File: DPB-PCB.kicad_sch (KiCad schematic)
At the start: 2 parts, among them J1 USB-C, U1 ESP32-S3-WROOM-1-N4R2

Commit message: up
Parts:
- removed J1: USB-C, Library:MOLEX_USB_TYPE_C, symbol MOLEX_USB_TYPE_C:105450-0101
- added Q1: MMBT5551L, Package_TO_SOT_SMD:SOT-23, symbol Transistor_BJT:MMBT5551L
- U1: LCSC (none) -> C2913204; MANUFACTURER Espressif -> (none); MAXIMUM_PACKAGE_HEIGHT 3.25mm -> (none); PARTREV v1.0 -> (none); STANDARD Manufacturer Recommendations -> (none)
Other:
- added sheet Connections (Connections.kicad_sch)
- added sheet Power Supply (PowerSupply.kicad_sch)
- company: (none) -> V2
- title: (none) -> Dynamic propeller balancer
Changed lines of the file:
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@@
 (kicad_sch (version 20230121) (generator eeschema)
   (paper "A4")
-  (symbol (lib_id "MOLEX_USB_TYPE_C:105450-0101") (at 74.93 82.55 0) (unit 1)
-    (in_bom yes) (on_board yes) (dnp no) (fields_autoplaced)
-    (property "Reference" "J1" (at 74.93 63.5 0)
-      (effects (font (size 1.27 1.27)))
-    )
-    (property "Value" "USB-C" (at 74.93 66.04 0)
-      (effects (font (size 1.27 1.27)))
-    )
-    (property "Footprint" "Library:MOLEX_USB_TYPE_C" (at 74.93 82.55 0)
-      (effects (font (size 1.27 1.27)) (justify bottom) hide)
-    )
-    (property "Datasheet" "" (at 74.93 82.55 0)
-      (effects (font (size 1.27 1.27)) hide)
-    )
-    (property "STANDARD" "Manufacturer Recommendations" (at 74.93 82.55 0)
-      (effects (font (size 1.27 1.27)) (justify bottom) hide)
-    )
-    (property "PARTREV" "A7" (at 74.93 82.55 0)
-      (effects (font (size 1.27 1.27)) (justify bottom) hide)
-    )
-    (property "MANUFACTURER" "Molex" (at 74.93 82.55 0)
-      (effects (font (size 1.27 1.27)) (justify bottom) hide)
-    )
-    (property "MAXIMUM_PACKAGE_HEIGHT" "3.24mm" (at 74.93 82.55 0)
-      (effects (font (size 1.27 1.27)) (justify bottom) hide)
-    )
-    (pin "A1")
-    (pin "A10")
-    (pin "A11")
-    (pin "A12")
-    (pin "A2")
-    (pin "A3")
-    (pin "A4")
-    (pin "A5")
-    (pin "A6")
-    (pin "A7")
-    (pin "A8")
-    (pin "A9")
-    (pin "B1")
-    (pin "B10")
-    (pin "B11")
-    (pin "B12")
-    (pin "B2")
-    (pin "B3")
-    (pin "B4")
-    (pin "B5")
-    (pin "B6")
-    (pin "B7")
-    (pin "B8")
-    (pin "B9")
-    (pin "S1")
-    (pin "S2")
-    (pin "S3")
-    (pin "S4")
-    (instances
-      (project "DPB-PCB"
-        (path "/0a09ce58-c923-4e96-b56b-0b86aca559ed"
-          (reference "J1") (unit 1)
-        )
-      )
-    )
+  (title_block
+    (title "Dynamic propeller balancer")
+    (date "2023-02-27")
+    (rev "1")
+    (company "V2")
   )
   (symbol (lib_id "ESP32-S3-WROOM-1-N4R2:ESP32-S3-WROOM-1-N4R2") (at 138.43 101.6 0) (unit 1)
@@
       (effects (font (size 1.27 1.27)) hide)
     )
-    (property "PARTREV" "v1.0" (at 138.43 101.6 0)
-      (effects (font (size 1.27 1.27)) (justify bottom) hide)
-    )
-    (property "MANUFACTURER" "Espressif" (at 138.43 101.6 0)
-      (effects (font (size 1.27 1.27)) (justify bottom) hide)
-    )
-    (property "MAXIMUM_PACKAGE_HEIGHT" "3.25mm" (at 138.43 101.6 0)
-      (effects (font (size 1.27 1.27)) (justify bottom) hide)
-    )
-    (property "STANDARD" "Manufacturer Recommendations" (at 138.43 101.6 0)
-      (effects (font (size 1.27 1.27)) (justify bottom) hide)
+    (property "LCSC" "C2913204" (at 138.43 101.6 0)
+      (effects (font (size 1.27 1.27)) hide)
     )
     (pin "1")
@@
       )
     )
+  )
+  (symbol (lib_id "Transistor_BJT:MMBT5551L") (at 189.23 81.28 0) (unit 1)
+    (in_bom yes) (on_board yes) (dnp no) (fields_autoplaced)
+    (property "Reference" "Q1" (at 194.31 80.645 0)
+      (effects (font (size 1.27 1.27)) (justify left))
+    )
+    (property "Value" "MMBT5551L" (at 194.31 83.185 0)
+      (effects (font (size 1.27 1.27)) (justify left))
+    )
+    (property "Footprint" "Package_TO_SOT_SMD:SOT-23" (at 194.31 83.185 0)
+      (effects (font (size 1.27 1.27) italic) (justify left) hide)
+    )
+    (property "Datasheet" "www.onsemi.com/pub/Collateral/MMBT5550LT1-D.PDF" (at 189.23 81.28 0)
+      (effects (font (size 1.27 1.27)) (justify left) hide)
+    )
+    (property "LCSC" "" (at 189.23 81.28 0)
+      (effects (font (size 1.27 1.27)) hide)
+    )
+    (pin "1")
+    (pin "2")
+    (pin "3")
+    (instances
+      (project "DPB-PCB"
+        (path "/0a09ce58-c923-4e96-b56b-0b86aca559ed"
+          (reference "Q1") (unit 1)
+        )
+      )
+    )
+  )
+  (sheet (at 17.78 17.78) (size 19.05 11.43) (fields_autoplaced)
+    (stroke (width 0.1524) (type solid))
+    (fill (color 0 0 0 0.0000))
+    (property "Sheetname" "Power Supply" (at 17.78 17.0684 0)
+      (effects (font (size 1.27 1.27)) (justify left bottom))
+    )
+    (property "Sheetfile" "PowerSupply.kicad_sch" (at 17.78 29.7946 0)
+      (effects (font (size 1.27 1.27)) (justify left top))
+    )
+    (instances
+      (project "DPB-PCB"
+        (path "/0a09ce58-c923-4e96-b56b-0b86aca559ed" (page "2"))
+      )
+    )
+  )
+  (sheet (at 53.34 17.78) (size 22.86 11.43) (fields_autoplaced)
+    (stroke (width 0.1524) (type solid))
+    (fill (color 0 0 0 0.0000))
+    (property "Sheetname" "Connections" (at 53.34 17.0684 0)
+      (effects (font (size 1.27 1.27)) (justify left bottom))
+    )
+    (property "Sheetfile" "Connections.kicad_sch" (at 53.34 29.7946 0)
+      (effects (font (size 1.27 1.27)) (justify left top))
+    )
+    (instances
+      (project "DPB-PCB"
+        (path "/0a09ce58-c923-4e96-b56b-0b86aca559ed" (page "3"))
+      )
+    )

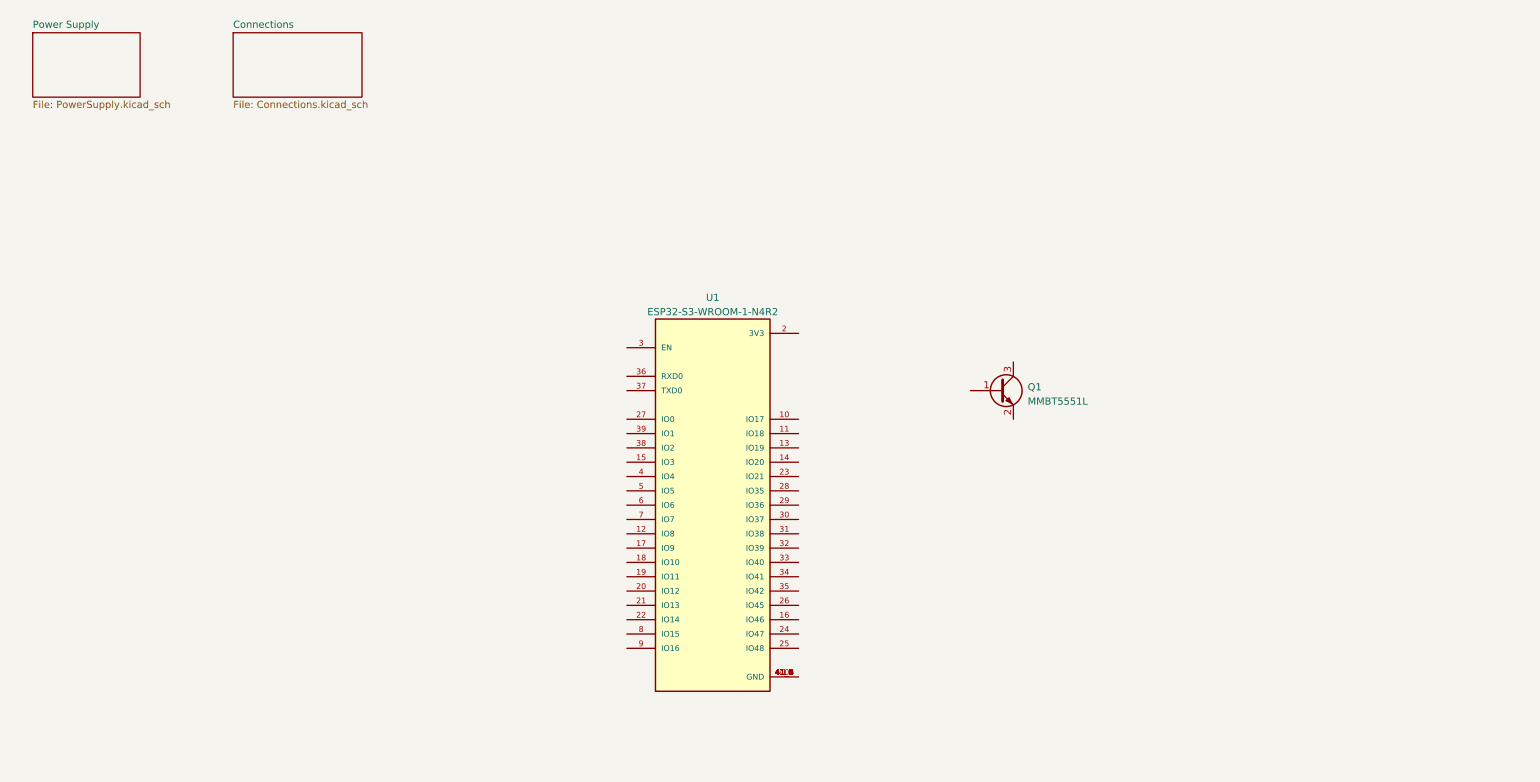
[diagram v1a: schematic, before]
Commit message: All components have been added
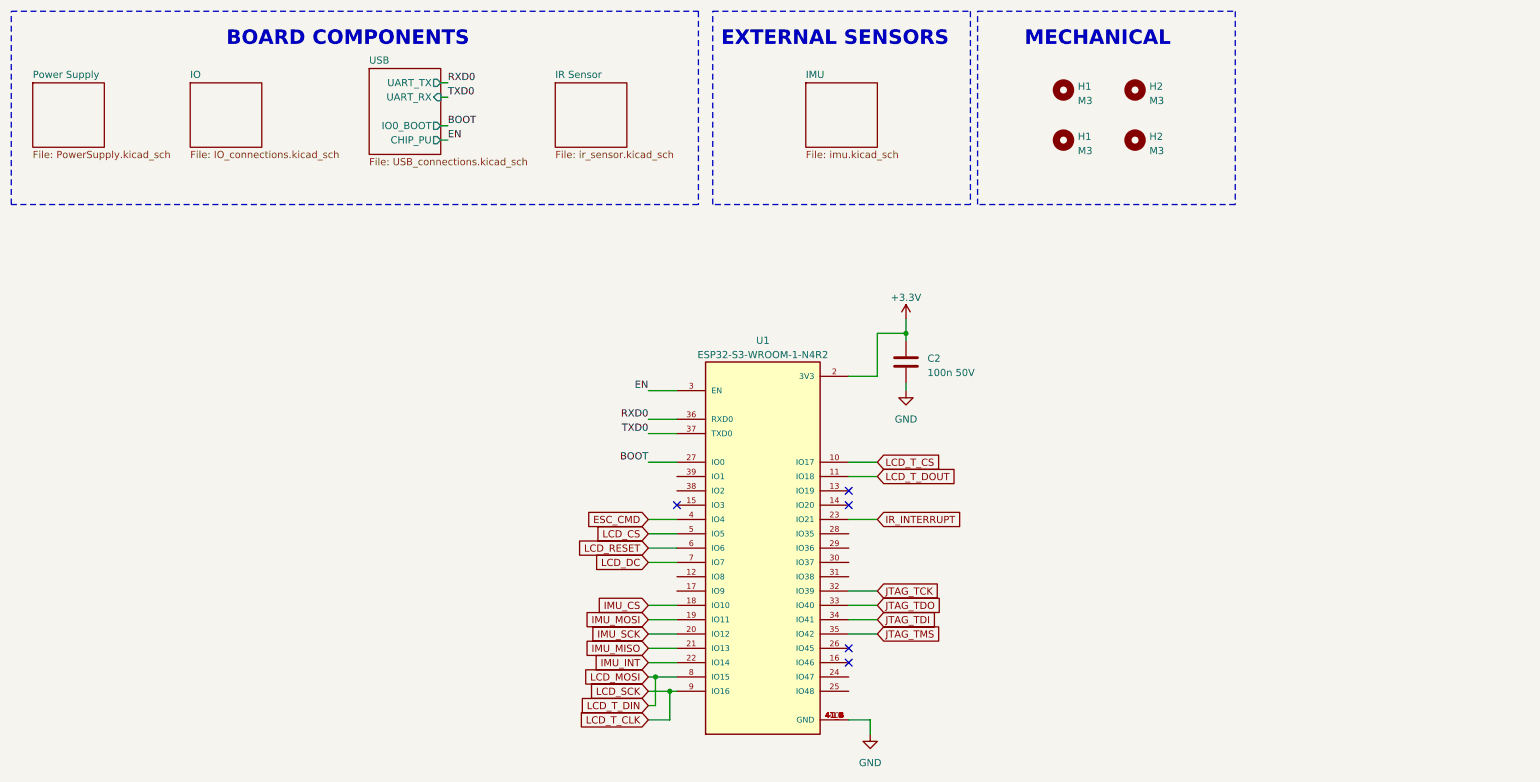
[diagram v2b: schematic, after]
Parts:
- removed Q1: MMBT5551L, Package_TO_SOT_SMD:SOT-23, symbol Transistor_BJT:MMBT5551L
- added C2: 100n 50V, Capacitor_SMD:C_01005_0402Metric, symbol Device:C
- added H1 (x2), H2 (x2): M3, MountingHole:MountingHole_3.2mm_M3_Pad_TopBottom, symbol Mechanical:MountingHole
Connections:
- net GND: now reaches U1.1 (GND), U1.40 (GND), U1.41_1 (GND), U1.41_2 (GND), U1.41_3 (GND), U1.41_4 (GND), U1.41_5 (GND), U1.41_6 (GND), U1.41_7 (GND), U1.41_8 (GND), U1.41_9 (GND)
- net GND: now also C2.2
- net LCD_T_CS: now reaches U1.10 (IO17)
- net LCD_T_DOUT: now reaches U1.11 (IO18)
- net IMU_CS: now reaches U1.18 (IO10)
- net IMU_MOSI: now reaches U1.19 (IO11)
- net +3.3V: now reaches U1.2 (3V3)
- net +3.3V: now also C2.1
- net IMU_SCK: now reaches U1.20 (IO12)
- net IMU_MISO: now reaches U1.21 (IO13)
- net IMU_INT: now reaches U1.22 (IO14)
- net IR_INTERRUPT: now reaches U1.23 (IO21)
- net BOOT: now reaches U1.27 (IO0)
- net EN: now reaches U1.3 (EN)
- net JTAG_TCK: now reaches U1.32 (IO39)
- net JTAG_TDO: now reaches U1.33 (IO40)
- net JTAG_TDI: now reaches U1.34 (IO41)
- net JTAG_TMS: now reaches U1.35 (IO42)
- net RXD0: now reaches U1.36 (RXD0)
- net TXD0: now reaches U1.37 (TXD0)
- net ESC_CMD: now reaches U1.4 (IO4)
- net LCD_CS: now reaches U1.5 (IO5)
- net LCD_RESET: now reaches U1.6 (IO6)
- net LCD_DC: now reaches U1.7 (IO7)
- net LCD_MOSI: now reaches U1.8 (IO15)
- net LCD_SCK: now reaches U1.9 (IO16)
- no-connect marks 0 -> 5
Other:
- sheet Connections renamed USB
- added sheet IMU (imu.kicad_sch)
- added sheet IO (IO_connections.kicad_sch)
- added sheet IR Sensor (ir_sensor.kicad_sch)
- sheet USB: file Connections.kicad_sch -> USB_connections.kicad_sch
- sheet USB ports: added CHIP_PU, IO0_BOOT, UART_RX, UART_TX; removed none
- note added: "BOARD COMPONENTS"
- note added: "EXTERNAL SENSORS"
- note added: "MECHANICAL"
- moved on the sheet: U1

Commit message: Divided project
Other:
- removed sheet IMU
- note removed: "EXTERNAL SENSORS"
- moved on the sheet: H1, H2
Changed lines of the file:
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@@
     (stroke (width 0) (type default))
   )
-  (rectangle (start 138.43 13.97) (end 184.15 48.26)
-    (stroke (width 0) (type dash))
-    (fill (type none))
-  )
-  (rectangle (start 185.42 13.97) (end 231.14 48.26)
+  (rectangle (start 137.16 13.97) (end 182.88 48.26)
     (stroke (width 0) (type dash))
     (fill (type none))
@@
     (fill (type none))
   )
-  (text "EXTERNAL SENSORS" (at 180.34 20.32 0)
-    (effects (font (size 2.5654 2.5654) (thickness 0.5131) bold) (justify right bottom))
-  )
-  (text "MECHANICAL" (at 219.71 20.32 0)
+  (text "MECHANICAL" (at 171.45 20.32 0)
     (effects (font (size 2.5654 2.5654) (thickness 0.5131) bold) (justify right bottom))
   )
@@
     )
   )
-  (symbol (lib_id "Mechanical:MountingHole") (at 213.36 27.94 0) (unit 1)
-    (in_bom yes) (on_board yes) (dnp no) (fields_autoplaced)
-    (property "Reference" "H2" (at 215.9 27.305 0)
-      (effects (font (size 1.27 1.27)) (justify left))
-    )
-    (property "Value" "M3" (at 215.9 29.845 0)
-      (effects (font (size 1.27 1.27)) (justify left))
-    )
-    (property "Footprint" "MountingHole:MountingHole_3.2mm_M3_Pad_TopBottom" (at 213.36 27.94 0)
-      (effects (font (size 1.27 1.27)) hide)
-    )
-    (property "Datasheet" "~" (at 213.36 27.94 0)
-      (effects (font (size 1.27 1.27)) hide)
-    )
-    (instances
-      (project "DPB-PCB"
-        (path "/0a09ce58-c923-4e96-b56b-0b86aca559ed/5d947656-d224-44e7-8ee3-5b0d738fb419"
-          (reference "H2") (unit 1)
-        )
+  (symbol (lib_id "Mechanical:MountingHole") (at 165.1 27.94 0) (unit 1)
+    (in_bom yes) (on_board yes) (dnp no) (fields_autoplaced)
+    (property "Reference" "H2" (at 167.64 27.305 0)
+      (effects (font (size 1.27 1.27)) (justify left))
+    )
+    (property "Value" "M3" (at 167.64 29.845 0)
+      (effects (font (size 1.27 1.27)) (justify left))
+    )
+    (property "Footprint" "MountingHole:MountingHole_3.2mm_M3_Pad_TopBottom" (at 165.1 27.94 0)
+      (effects (font (size 1.27 1.27)) hide)
+    )
+    (property "Datasheet" "~" (at 165.1 27.94 0)
+      (effects (font (size 1.27 1.27)) hide)
+    )
+    (instances
+      (project "DPB-PCB"
         (path "/0a09ce58-c923-4e96-b56b-0b86aca559ed"
           (reference "H4") (unit 1)
@@
     )
   )
-  (symbol (lib_id "Mechanical:MountingHole") (at 200.66 36.83 0) (unit 1)
-    (in_bom yes) (on_board yes) (dnp no) (fields_autoplaced)
-    (property "Reference" "H1" (at 203.2 36.195 0)
-      (effects (font (size 1.27 1.27)) (justify left))
-    )
-    (property "Value" "M3" (at 203.2 38.735 0)
-      (effects (font (size 1.27 1.27)) (justify left))
-    )
-    (property "Footprint" "MountingHole:MountingHole_3.2mm_M3_Pad_TopBottom" (at 200.66 36.83 0)
-      (effects (font (size 1.27 1.27)) hide)
-    )
-    (property "Datasheet" "~" (at 200.66 36.83 0)
-      (effects (font (size 1.27 1.27)) hide)
-    )
-    (instances
-      (project "DPB-PCB"
-        (path "/0a09ce58-c923-4e96-b56b-0b86aca559ed/5d947656-d224-44e7-8ee3-5b0d738fb419"
-          (reference "H1") (unit 1)
-        )
+  (symbol (lib_id "Mechanical:MountingHole") (at 152.4 36.83 0) (unit 1)
+    (in_bom yes) (on_board yes) (dnp no) (fields_autoplaced)
+    (property "Reference" "H1" (at 154.94 36.195 0)
+      (effects (font (size 1.27 1.27)) (justify left))
+    )
+    (property "Value" "M3" (at 154.94 38.735 0)
+      (effects (font (size 1.27 1.27)) (justify left))
+    )
+    (property "Footprint" "MountingHole:MountingHole_3.2mm_M3_Pad_TopBottom" (at 152.4 36.83 0)
+      (effects (font (size 1.27 1.27)) hide)
+    )
+    (property "Datasheet" "~" (at 152.4 36.83 0)
+      (effects (font (size 1.27 1.27)) hide)
+    )
+    (instances
+      (project "DPB-PCB"
         (path "/0a09ce58-c923-4e96-b56b-0b86aca559ed"
           (reference "H5") (unit 1)
@@
     )
   )
-  (symbol (lib_id "Mechanical:MountingHole") (at 213.36 36.83 0) (unit 1)
-    (in_bom yes) (on_board yes) (dnp no) (fields_autoplaced)
-    (property "Reference" "H2" (at 215.9 36.195 0)
-      (effects (font (size 1.27 1.27)) (justify left))
-    )
-    (property "Value" "M3" (at 215.9 38.735 0)
-      (effects (font (size 1.27 1.27)) (justify left))
-    )
-    (property "Footprint" "MountingHole:MountingHole_3.2mm_M3_Pad_TopBottom" (at 213.36 36.83 0)
-      (effects (font (size 1.27 1.27)) hide)
-    )
-    (property "Datasheet" "~" (at 213.36 36.83 0)
-      (effects (font (size 1.27 1.27)) hide)
-    )
-    (instances
-      (project "DPB-PCB"
-        (path "/0a09ce58-c923-4e96-b56b-0b86aca559ed/5d947656-d224-44e7-8ee3-5b0d738fb419"
-          (reference "H2") (unit 1)
-        )
+  (symbol (lib_id "Mechanical:MountingHole") (at 165.1 36.83 0) (unit 1)
+    (in_bom yes) (on_board yes) (dnp no) (fields_autoplaced)
+    (property "Reference" "H2" (at 167.64 36.195 0)
+      (effects (font (size 1.27 1.27)) (justify left))
+    )
+    (property "Value" "M3" (at 167.64 38.735 0)
+      (effects (font (size 1.27 1.27)) (justify left))
+    )
+    (property "Footprint" "MountingHole:MountingHole_3.2mm_M3_Pad_TopBottom" (at 165.1 36.83 0)
+      (effects (font (size 1.27 1.27)) hide)
+    )
+    (property "Datasheet" "~" (at 165.1 36.83 0)
+      (effects (font (size 1.27 1.27)) hide)
+    )
+    (instances
+      (project "DPB-PCB"
         (path "/0a09ce58-c923-4e96-b56b-0b86aca559ed"
           (reference "H6") (unit 1)
@@
     )
   )
-  (symbol (lib_id "Mechanical:MountingHole") (at 200.66 27.94 0) (unit 1)
-    (in_bom yes) (on_board yes) (dnp no) (fields_autoplaced)
-    (property "Reference" "H1" (at 203.2 27.305 0)
-      (effects (font (size 1.27 1.27)) (justify left))
-    )
-    (property "Value" "M3" (at 203.2 29.845 0)
-      (effects (font (size 1.27 1.27)) (justify left))
-    )
-    (property "Footprint" "MountingHole:MountingHole_3.2mm_M3_Pad_TopBottom" (at 200.66 27.94 0)
-      (effects (font (size 1.27 1.27)) hide)
-    )
-    (property "Datasheet" "~" (at 200.66 27.94 0)
-      (effects (font (size 1.27 1.27)) hide)
-    )
-    (instances
-      (project "DPB-PCB"
-        (path "/0a09ce58-c923-4e96-b56b-0b86aca559ed/5d947656-d224-44e7-8ee3-5b0d738fb419"
-          (reference "H1") (unit 1)
-        )
+  (symbol (lib_id "Mechanical:MountingHole") (at 152.4 27.94 0) (unit 1)
+    (in_bom yes) (on_board yes) (dnp no) (fields_autoplaced)
+    (property "Reference" "H1" (at 154.94 27.305 0)
+      (effects (font (size 1.27 1.27)) (justify left))
+    )
+    (property "Value" "M3" (at 154.94 29.845 0)
+      (effects (font (size 1.27 1.27)) (justify left))
+    )
+    (property "Footprint" "MountingHole:MountingHole_3.2mm_M3_Pad_TopBottom" (at 152.4 27.94 0)
+      (effects (font (size 1.27 1.27)) hide)
+    )
+    (property "Datasheet" "~" (at 152.4 27.94 0)
+      (effects (font (size 1.27 1.27)) hide)
+    )
+    (instances
+      (project "DPB-PCB"
         (path "/0a09ce58-c923-4e96-b56b-0b86aca559ed"
           (reference "H3") (unit 1)
@@
       )
     )
-  )
-  (sheet (at 154.94 26.67) (size 12.7 11.43) (fields_autoplaced)
-    (stroke (width 0.1524) (type solid))
-    (fill (color 0 0 0 0.0000))
-    (property "Sheetname" "IMU" (at 154.94 25.9584 0)
-      (effects (font (size 1.27 1.27)) (justify left bottom))
-    )
-    (property "Sheetfile" "imu.kicad_sch" (at 154.94 38.6846 0)
-      (effects (font (size 1.27 1.27)) (justify left top))
-    )
-    (instances
-      (project "DPB-PCB"
-        (path "/0a09ce58-c923-4e96-b56b-0b86aca559ed" (page "5"))
-      )
-    )

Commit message: DPB mainboard_v1 completed
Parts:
- added R3 (x7): 47, Resistor_SMD:R_0402_1005Metric, symbol Device:R
- added R3 (x2): 100, Resistor_SMD:R_0402_1005Metric, symbol Device:R
- renumbered H1 to H2, H2 to H3, H2 to H4
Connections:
- net GND: now also U1.41 (GND); no longer U1.41_1 (GND), U1.41_2 (GND), U1.41_3 (GND), U1.41_4 (GND), U1.41_5 (GND), U1.41_6 (GND), U1.41_7 (GND), U1.41_8 (GND), U1.41_9 (GND)
- net IMU_CS: now also R3.1; no longer U1.18 (IO10)
- net IMU_MISO: now also U1.20 (IO12); no longer U1.21 (IO13)
- net IMU_MOSI: now also R3.2; no longer U1.19 (IO11)
- net IMU_SCK: now also R3.2; no longer U1.20 (IO12)
- net LCD_CS: now also R3.2; no longer U1.5 (IO5)
- net LCD_DC: now also R3.2; no longer U1.7 (IO7)
- net LCD_MOSI: now also R3.2; no longer U1.8 (IO15)
- net LCD_RESET: now also R3.2; no longer U1.6 (IO6)
- net LCD_SCK: now also R3.2; no longer U1.9 (IO16)
- net LCD_T_CS: now also R3.1; no longer U1.10 (IO17)
- net USB_D-: now reaches U1.13 (IO19)
- net USB_D+: now reaches U1.14 (IO20)
- net GPIO47: now reaches U1.24 (IO47)
- net GPIO47: now also R3.2
- net JTAG_TCK: no longer names the net of U1.32 (IO39)
- net JTAG_TDI: no longer names the net of U1.34 (IO41)
- net JTAG_TDO: no longer names the net of U1.33 (IO40)
- net JTAG_TMS: no longer names the net of U1.35 (IO42)
- net LCD_T_DOUT renamed GPIO18
- net GPIO18: now also R3.2
- new net GPIO11: R3.1, U1.19 (IO11)
- new net GPIO13: R3.1, U1.21 (IO13)
- new net GPIO15: R3.1, U1.8 (IO15)
- new net GPIO16: R3.1, U1.9 (IO16)
- new net GPIO5: R3.1, U1.5 (IO5)
- new net GPIO6: R3.1, U1.6 (IO6)
- new net GPIO7: R3.1, U1.7 (IO7)
- new net LCD_MISO: U1.10 (IO17)
- new net V_ADC2: U1.18 (IO10)
- no-connect marks 5 -> 16
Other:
- added sheet USB OTG (USB_OTG_connections.kicad_sch)
- moved on the sheet: H1, H2, H3, H4
